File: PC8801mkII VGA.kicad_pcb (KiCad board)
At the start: 2 copper layers, 39.4 x 31.8 mm, 5 parts

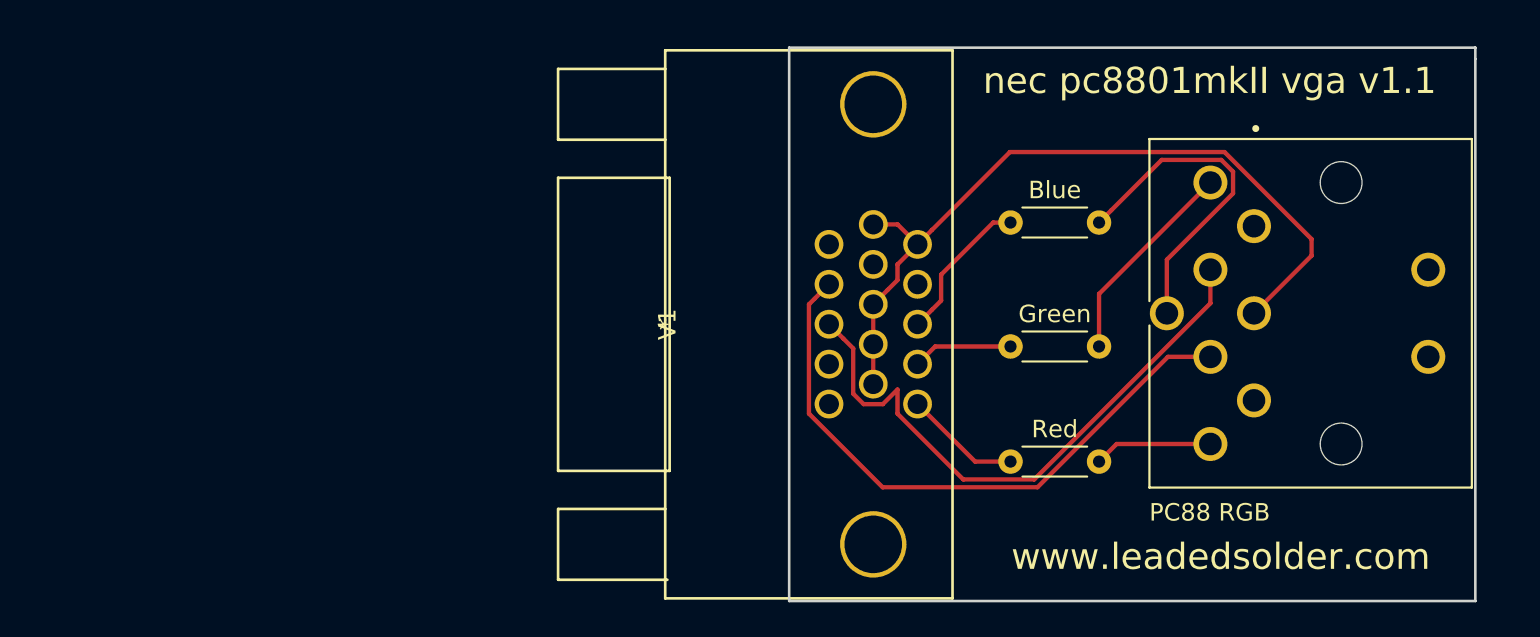
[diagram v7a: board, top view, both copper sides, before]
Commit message: Now with easier-to-cut sync traces
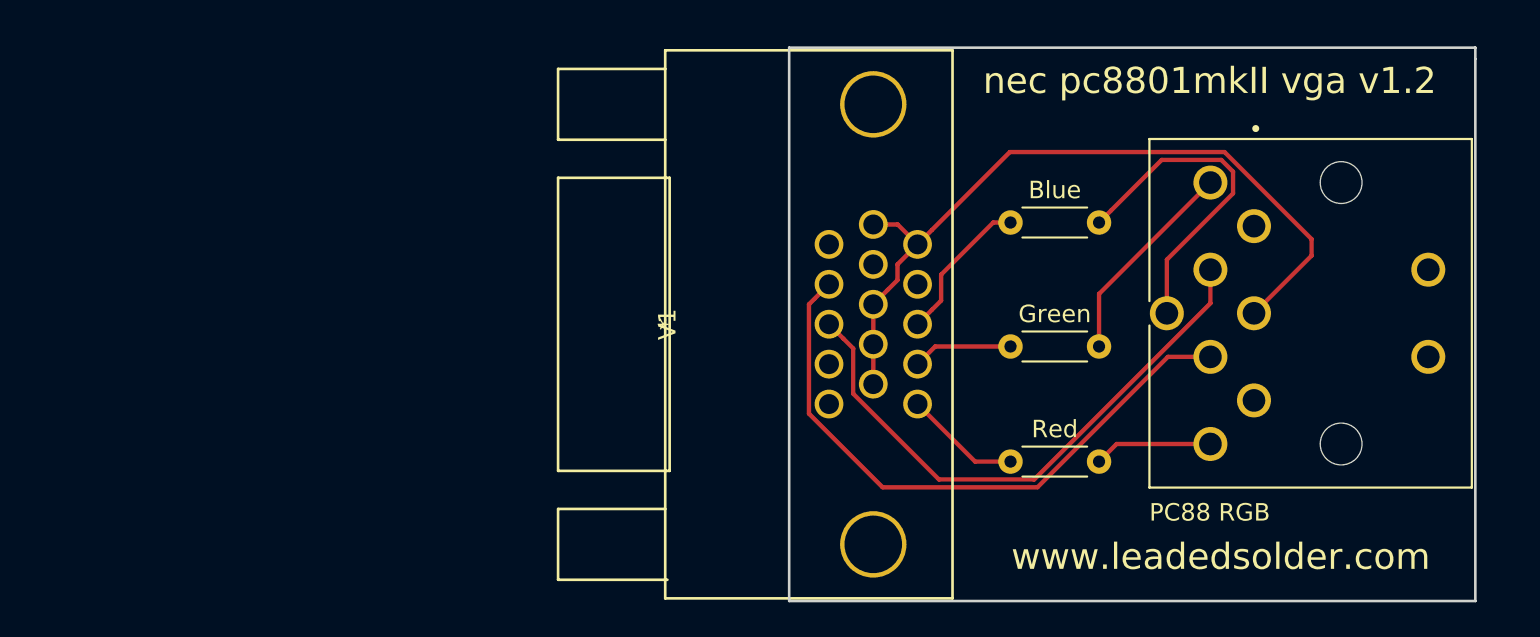
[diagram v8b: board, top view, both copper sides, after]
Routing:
- net /V-Sync: track 34.7 -> 33.2 mm
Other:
- board text added: "nec pc8801mkII vga v1.2"
- board text removed: "nec pc8801mkII vga v1.1"
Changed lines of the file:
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@@
     (thickness 1.6)
     (drawings 9)
-    (tracks 52)
+    (tracks 48)
     (zones 0)
     (modules 5)
@@
     (effects (font (size 1.5 1.5) (thickness 0.3)) (justify mirror))
   )
-  (gr_text "nec pc8801mkII vga v1.1" (at 199.39 93.98) (layer F.SilkS)
+  (gr_text "nec pc8801mkII vga v1.2" (at 199.39 93.98) (layer F.SilkS)
     (effects (font (size 1.5 1.5) (thickness 0.3)))
   )
@@
   (segment (start 189.506401 117.299011) (end 180.620269 117.299011) (width 0.25) (layer F.Cu) (net 4))
   (segment (start 199.43 109.815) (end 196.990412 109.815) (width 0.25) (layer F.Cu) (net 4))
-  (segment (start 178.371499 108.767498) (end 177.546 107.941999) (width 0.25) (layer F.Cu) (net 5))
   (segment (start 178.935499 109.331498) (end 178.371499 108.767498) (width 0.25) (layer F.Cu) (net 5))
   (segment (start 178.935499 111.931241) (end 178.935499 109.331498) (width 0.25) (layer F.Cu) (net 5))
-  (segment (start 179.533759 112.529501) (end 178.935499 111.931241) (width 0.25) (layer F.Cu) (net 5))
-  (segment (start 180.638241 112.529501) (end 179.533759 112.529501) (width 0.25) (layer F.Cu) (net 5))
-  (segment (start 181.475499 111.692243) (end 180.638241 112.529501) (width 0.25) (layer F.Cu) (net 5))
-  (segment (start 181.475499 113.074241) (end 181.475499 111.692243) (width 0.25) (layer F.Cu) (net 5))
-  (segment (start 185.250259 116.849001) (end 181.475499 113.074241) (width 0.25) (layer F.Cu) (net 5))
-  (segment (start 189.320001 116.849001) (end 185.250259 116.849001) (width 0.25) (layer F.Cu) (net 5))
+  (segment (start 183.853259 116.849001) (end 178.935499 111.931241) (width 0.25) (layer F.Cu) (net 5))
+  (segment (start 189.320001 116.849001) (end 183.853259 116.849001) (width 0.25) (layer F.Cu) (net 5))
+  (segment (start 178.371499 108.767498) (end 177.546 107.941999) (width 0.25) (layer F.Cu) (net 5))
   (segment (start 199.43 106.739002) (end 189.320001 116.849001) (width 0.25) (layer F.Cu) (net 5))
   (segment (start 199.43 104.815) (end 199.43 106.739002) (width 0.25) (layer F.Cu) (net 5))
